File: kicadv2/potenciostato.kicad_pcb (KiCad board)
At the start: 2 copper layers, 100 x 100 mm, 57 parts, among them J1 USB_B_Micro, J10 test_GND, J11 test_GND, J12 test_GND, J2 test_DAC, J3 Conn_01x03_Male, J4 test_I, J5 test_V, J6 test_DAC, J7 test_I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

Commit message: trazando pcb
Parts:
- removed the R16 at (170.6, 134.4)
- removed the R16 at (155.0, 79.9)
- added J13: AC2, Connector_PinHeader_1.00mm:PinHeader_1x01_P1.00mm_Vertical, F.Cu at (120.7, 66.3)
- added J9: AC1, Connector_PinHeader_1.00mm:PinHeader_1x01_P1.00mm_Vertical, F.Cu at (120.7, 61.2)
- added R16: 10K, Resistor_SMD:R_1206_3216Metric_Pad1.30x1.75mm_HandSolder, B.Cu at (212.6, 69.6)
- C3, C4, D1, R17, R19, R20, TR1: moved to B.Cu
- moved RV1 106.1 mm to (192.3, 63.0), turned to 90 degrees
- moved J3 90.9 mm to (149.0, 151.1), turned to 180 degrees
- moved JP1 80.1 mm to (165.9, 152.4), turned to 180 degrees
- moved R17 75.3 mm to (185.6, 63.0), turned to 180 degrees
- moved R19 75.3 mm to (185.6, 68.1)
- moved U9 70.0 mm to (200.5, 60.5)
- moved R23 68.2 mm to (121.4, 120.1), turned to 90 degrees
- moved J10 66.4 mm to (123.7, 147.3)
- moved J4 58.7 mm to (133.1, 138.2)
- moved C3 58.0 mm to (160.3, 60.3)
- moved J12 57.2 mm to (133.1, 142.7)
- moved C4 56.8 mm to (172.4, 60.3)
- moved U5 50.3 mm to (171.4, 84.1)
- moved R18 49.2 mm to (121.4, 126.2), turned to 90 degrees
- moved R20 45.6 mm to (212.6, 63.3), turned to 270 degrees
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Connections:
- U7 pad 14: Net-(U7-Pad12) -> Net-(U7-Pad14)
- U9 pad 6: /salida_dac/-VOffset -> GND
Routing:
- net Net-(C2-Pad2): track 0.00 -> 46.9 mm
- net Net-(C1-Pad1): track 0.00 -> 22.2 mm
- net /salida_dac/VOffset: track 0.00 -> 19.4 mm
- net Net-(D1-Pad4): track 0.00 -> 14.0 mm
- net Net-(D1-Pad3): track 0.00 -> 11.3 mm
- net Net-(RV1-Pad2): track 0.00 -> 8.25 mm
- net Net-(R16-Pad1): track 0.00 -> 7.62 mm
- net -5V: track 0.00 -> 7.50 mm
- net +5V: track 0.00 -> 7.49 mm
- net Net-(J9-Pad1): track 0.00 -> 5.84 mm
- net Net-(J13-Pad1): track 0.00 -> 5.84 mm
- net Net-(R19-Pad2): track 0.00 -> 5.08 mm
- net Net-(R17-Pad1): track 0.00 -> 5.08 mm
- net /salida_dac/-VOffset: track 0.00 -> 4.94 mm

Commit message: trazado pcb
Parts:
- moved JP1 76.1 mm to (179.1, 77.5), turned to 0 degrees
- moved D2 51.6 mm to (121.7, 118.1)
- moved R7 51.6 mm to (127.7, 118.1)
- moved R1 50.8 mm to (169.5, 135.0), turned to 90 degrees
- moved R15 45.3 mm to (166.4, 135.0), turned to 90 degrees
- moved R4 43.7 mm to (166.4, 146.4), turned to 90 degrees
- moved D3 40.1 mm to (127.4, 121.9)
- moved R14 39.6 mm to (91.9, 129.0)
- moved R18 39.6 mm to (82.0, 122.4)
- moved R23 39.6 mm to (82.0, 116.3)
- moved R9 39.6 mm to (85.3, 129.0)
- moved R13 39.6 mm to (101.1, 110.2)
- moved R2 39.6 mm to (101.1, 116.6)
- moved R3 39.6 mm to (107.2, 118.1)
- moved U7 39.6 mm to (87.4, 108.5)
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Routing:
- net Net-(R1-Pad1): track 0.00 -> 19.1 mm
- net Net-(R1-Pad2): track 0.00 -> 19.0 mm
- net Net-(J3-Pad1): track 0.00 -> 18.9 mm
- net Net-(R4-Pad1): track 0.00 -> 12.9 mm
- net Net-(R12-Pad2): track 0.00 -> 8.64 mm
- net Net-(R11-Pad2): track 0.00 -> 7.06 mm

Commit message: trazado pcb
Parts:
- moved U3 38.2 mm to (146.1, 136.5)
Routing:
- net Net-(R15-Pad2): track 0.00 -> 26.9 mm
- net /salida_dac/I_IN: track 0.00 -> 2.54 mm
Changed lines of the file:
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@@
     (thickness 1.6)
     (drawings 5)
-    (tracks 57)
+    (tracks 66)
     (zones 0)
     (modules 58)
@@
   )
   (module Package_SO:HSOP-8-1EP_3.9x4.9mm_P1.27mm_EP2.41x3.1mm (layer F.Cu)
-    (at 172.72 109.22)
+    (at 146.05 136.525)
     (descr "HSOP, 8 Pin (https://www.st.com/resource/en/datasheet/l5973d.pdf), generated with kicad-footprint-generator ipc_gullwing_generator.py")
     (tags "HSOP SO")
@@
   (segment (start 156.21 140.97) (end 153.487 143.693) (width 0.508) (layer F.Cu) (net 15))
   (segment (start 159.46 140.97) (end 156.21 140.97) (width 0.508) (layer F.Cu) (net 15))
-  (segment (start 169.545 133.425) (end 173.99 128.98) (width 0.508) (layer F.Cu) (net 24))
-  (segment (start 173.99 128.98) (end 173.99 120.015) (width 0.508) (layer F.Cu) (net 24))
-  (segment (start 172.72 118.745) (end 170.815 118.745) (width 0.508) (layer F.Cu) (net 24))
-  (segment (start 173.99 120.015) (end 172.72 118.745) (width 0.508) (layer F.Cu) (net 24))
+  (segment (start 165.735 118.745) (end 168.275 118.745) (width 0.508) (layer F.Cu) (net 18))
+  (segment (start 175.26 123.19) (end 170.815 118.745) (width 0.508) (layer F.Cu) (net 24))
+  (segment (start 175.26 127.71) (end 175.26 123.19) (width 0.508) (layer F.Cu) (net 24))
+  (segment (start 169.545 133.425) (end 175.26 127.71) (width 0.508) (layer F.Cu) (net 24))
   (segment (start 166.37 144.855) (end 166.37 136.525) (width 0.508) (layer F.Cu) (net 25))
   (segment (start 159.385 136.525) (end 170.18 136.525) (width 0.508) (layer F.Cu) (net 25))
@@
   (segment (start 155.575 129.615) (end 155.575 126.365) (width 0.508) (layer F.Cu) (net 34))
   (segment (start 159.385 133.425) (end 155.575 129.615) (width 0.508) (layer F.Cu) (net 34))
+  (segment (start 163.195 120.453) (end 163.195 118.745) (width 0.508) (layer F.Cu) (net 35))
+  (segment (start 164.027 121.285) (end 163.195 120.453) (width 0.508) (layer F.Cu) (net 35))
+  (segment (start 170.18 121.285) (end 164.027 121.285) (width 0.508) (layer F.Cu) (net 35))
+  (segment (start 173.355 124.46) (end 170.18 121.285) (width 0.508) (layer F.Cu) (net 35))
+  (segment (start 173.355 127.635) (end 173.355 124.46) (width 0.508) (layer F.Cu) (net 35))
+  (segment (start 170.815 130.175) (end 173.355 127.635) (width 0.508) (layer F.Cu) (net 35))
+  (segment (start 168.3125 130.175) (end 170.815 130.175) (width 0.508) (layer F.Cu) (net 35))
+  (segment (start 166.37 132.1175) (end 168.3125 130.175) (width 0.508) (layer F.Cu) (net 35))
+  (segment (start 166.37 133.425) (end 166.37 132.1175) (width 0.508) (layer F.Cu) (net 35))
   (segment (start 187.198 62.992) (end 192.278 62.992) (width 0.508) (layer B.Cu) (net 36))
   (segment (start 187.198 68.072) (end 192.278 68.072) (width 0.508) (layer B.Cu) (net 37))

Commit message: trazado casi listo
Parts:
- removed D2, D3: 1N4007, Diode_SMD:D_1206_3216Metric_Pad1.42x1.75mm_HandSolder
- J10, J11, J12, J13, J4, J5, J6, J7, J8, J9: footprint Connector_PinHeader_1.00mm:PinHeader_1x01_P1.00mm_Vertical -> Connector_PinHeader_2.54mm:PinHeader_1x01_P2.54mm_Vertical
- R16, R17, R19, R20: moved to F.Cu
- moved U9 110.0 mm to (120.7, 136.1), turned to 90 degrees
- moved R20 109.0 mm to (122.0, 124.0), turned to 0 degrees
- moved R17 105.5 mm to (127.3, 150.9), turned to 270 degrees
- moved R19 104.4 mm to (122.2, 150.9), turned to 90 degrees
- moved RV1 104.1 mm to (127.3, 144.3), turned to 0 degrees
- moved R16 100.3 mm to (128.3, 124.0), turned to 0 degrees
- moved R9 79.3 mm to (155.2, 91.4), turned to 90 degrees
- moved R14 77.0 mm to (167.1, 112.5), turned to 270 degrees
- moved J10 75.9 mm to (150.4, 76.3)
- moved R18 75.0 mm to (156.5, 113.0), turned to 180 degrees
- moved R23 74.7 mm to (156.5, 109.7), turned to 0 degrees
- moved J7 67.5 mm to (155.2, 76.3)
- moved R2 52.9 mm to (150.7, 135.0)
- moved R13 51.7 mm to (146.6, 134.9)
- moved R3 50.5 mm to (154.7, 135.0), turned to 90 degrees
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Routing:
- net GND: track 0.00 -> 519.0 mm, vias 0 -> 18
- net +5V: track 7.49 -> 281.0 mm, vias 0 -> 9
- net -5V: track 7.50 -> 241.6 mm, vias 0 -> 8
- net /salida_dac/3V3: track 0.00 -> 160.4 mm, vias 0 -> 2
- net /salida_dac/gan_x10: track 0.00 -> 144.3 mm, vias 0 -> 2
- net /salida_dac/gan_x0.1: track 0.00 -> 139.6 mm, vias 0 -> 2
- net /salida_dac/gan_x5: track 0.00 -> 130.4 mm, vias 0 -> 2
- net /salida_dac/gan_x1: track 0.00 -> 129.5 mm, vias 0 -> 2
- net Net-(J1-Pad2): track 0.00 -> 109.0 mm, vias 0 -> 2
- net Net-(J1-Pad3): track 0.00 -> 107.5 mm, vias 0 -> 2
- net Net-(J7-Pad1): track 0.00 -> 74.2 mm, vias 0 -> 3
- net Net-(J8-Pad1): track 0.00 -> 60.3 mm, vias 0 -> 2
- net /salida_dac/VIN: track 0.00 -> 57.6 mm
- net Net-(J2-Pad1): track 0.00 -> 54.5 mm, vias 0 -> 2
- net /salida_dac/I_IN: track 2.54 -> 52.9 mm
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
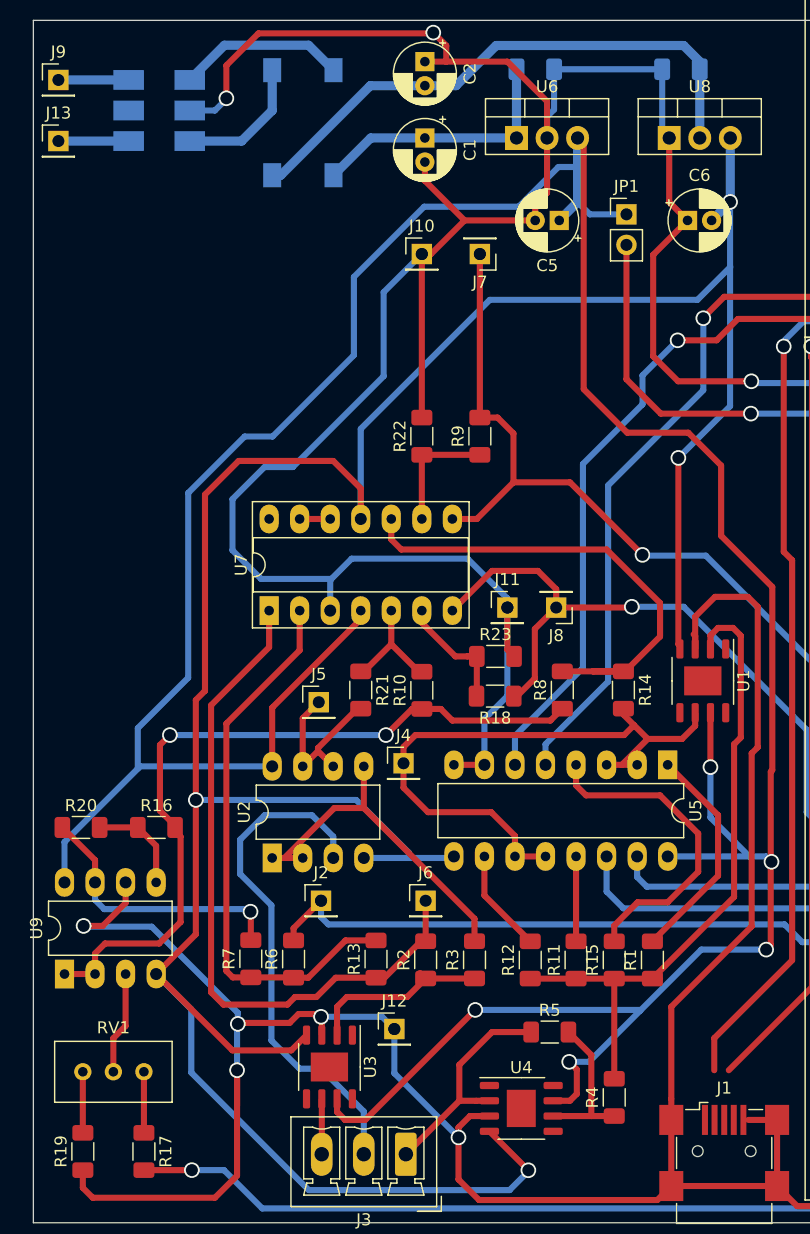
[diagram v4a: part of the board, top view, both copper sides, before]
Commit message: agregadas vias
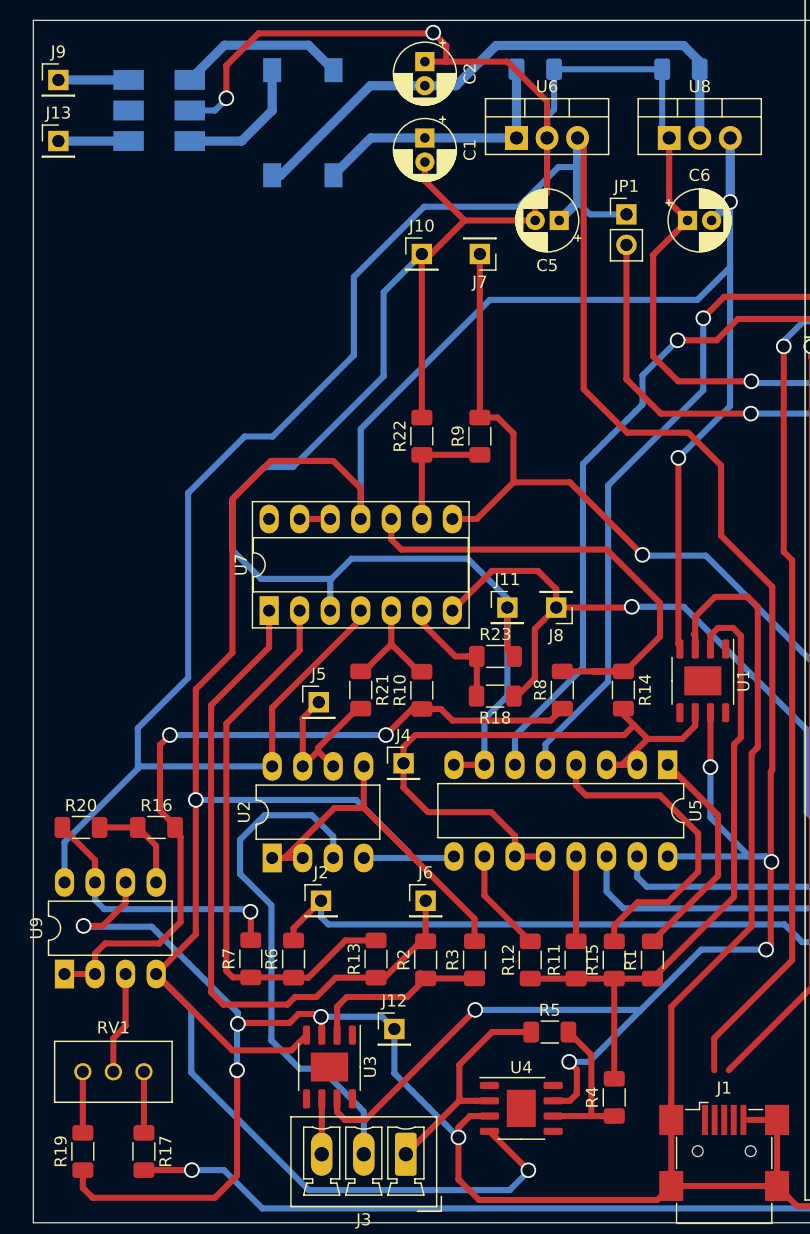
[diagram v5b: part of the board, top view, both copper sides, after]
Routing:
- net -5V: track 241.6 -> 240.0 mm, vias 8 -> 9
- net /salida_dac/VOffset: vias 2 -> 4
- net Net-(R10-Pad2): vias 0 -> 1
- net Net-(U7-Pad14): vias 0 -> 1
- net Net-(U7-Pad12): vias 0 -> 2
- net Net-(RV1-Pad2): vias 0 -> 2
- net Net-(R3-Pad2): vias 0 -> 3
- net Net-(R22-Pad1): vias 0 -> 1
- net Net-(R19-Pad2): vias 0 -> 1
- net Net-(R18-Pad2): vias 0 -> 1
- net Net-(R17-Pad1): vias 0 -> 1
- net Net-(R16-Pad1): vias 0 -> 1
- net Net-(R15-Pad2): vias 0 -> 1
- net Net-(R14-Pad1): vias 0 -> 1
- net Net-(R13-Pad2): vias 0 -> 1
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
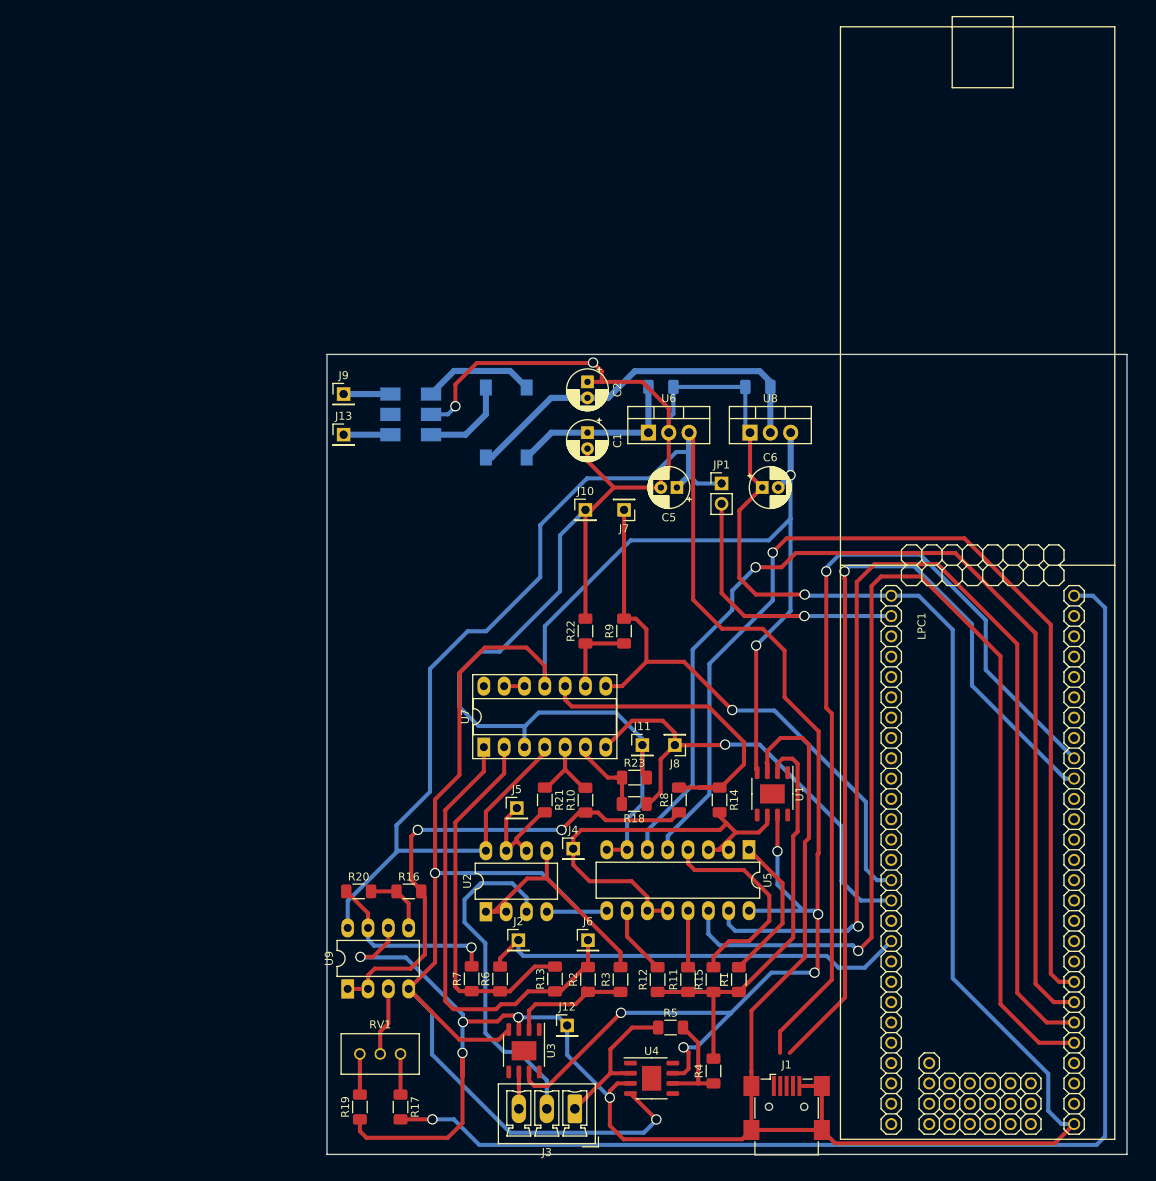
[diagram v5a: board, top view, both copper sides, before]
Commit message: puestos USBy trafo OK
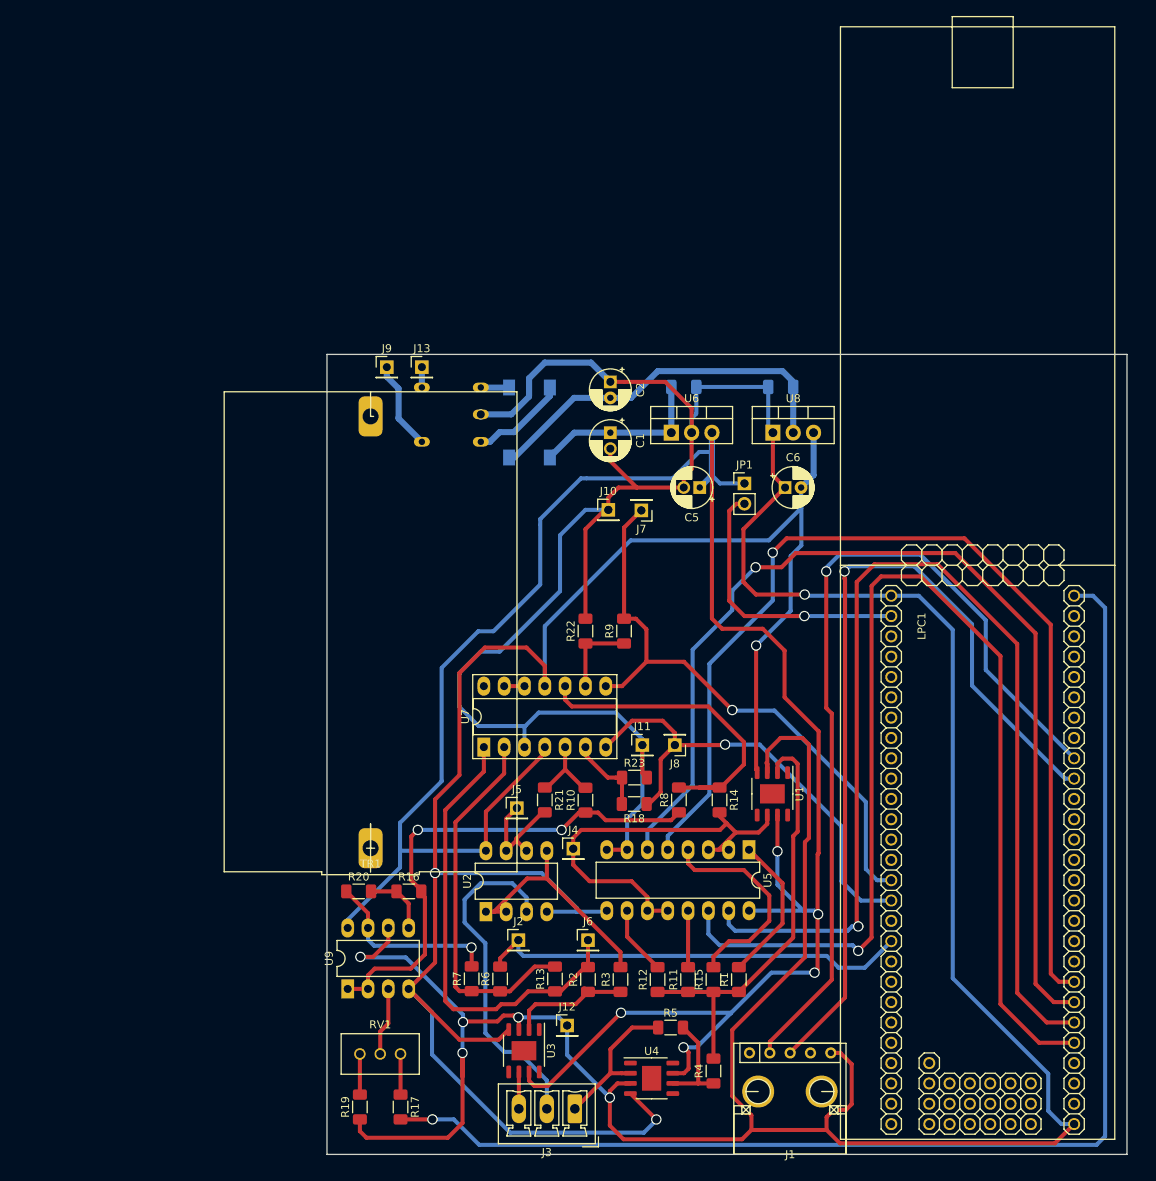
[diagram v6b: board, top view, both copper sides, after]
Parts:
- J1: footprint Connector_USB:USB_Mini-B_Wuerth_65100516121_Horizontal -> kicadv2:ModuloUSB-Micro
- TR1: footprint RF_Mini-Circuits:Mini-Circuits_CD637_H5.23mm -> kicadv2:Transformador_7.5V; moved to F.Cu
- moved TR1 27.6 mm to (123.5, 91.5), turned to 270 degrees
- moved J13 12.9 mm to (129.9, 58.4)
- moved J1 6.75 mm to (176.0, 144.1)
- moved J9 6.36 mm to (125.5, 58.4)
- moved D1 2.90 mm to (143.4, 65.3)
- moved C3 2.86 mm to (162.7, 60.9)
- moved J10 2.86 mm to (153.2, 76.3)
- moved JP1 2.86 mm to (170.2, 73.0)
- moved U6 2.86 mm to (161.1, 66.6)
- moved C1 2.86 mm to (153.5, 66.6)
- moved C2 2.86 mm to (153.5, 60.3)
- moved C4 2.86 mm to (174.8, 60.9)
- moved C5 2.86 mm to (164.7, 73.5)
- moved C6 2.86 mm to (175.3, 73.5)
- moved U8 2.86 mm to (173.8, 66.6)
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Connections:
- J1 pad 6: GND -> Net-(J1-Pad6)
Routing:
- net Net-(D1-Pad3): track 11.3 -> 3.54 mm
- net GND: track 519.0 -> 526.2 mm, vias 19 -> 22
- net Net-(J9-Pad1): track 5.84 -> 11.1 mm, vias 1 -> 0
- net Net-(J13-Pad1): track 5.84 -> 2.54 mm, vias 1 -> 0
- net +5V: track 281.0 -> 283.0 mm
- net Net-(D1-Pad4): track 14.0 -> 12.1 mm
- net Net-(JP1-Pad2): track 33.6 -> 34.6 mm
- net -5V: track 240.0 -> 240.9 mm, vias 9 -> 8
- net Net-(J7-Pad1): track 74.2 -> 75.0 mm
- net Net-(J1-Pad2): track 109.0 -> 109.6 mm
- net /salida_dac/gan_x5: vias 2 -> 3
- net /salida_dac/gan_x10: vias 2 -> 3
- net /salida_dac/gan_x1: vias 2 -> 3
- net /salida_dac/gan_x0.1: vias 2 -> 3
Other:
- net class Default: clearance 0.7 -> 0.35
- rule trace_clearance: 0.7 -> 0.35
